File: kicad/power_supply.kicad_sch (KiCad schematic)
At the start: 14 parts, among them U3 LMR38010

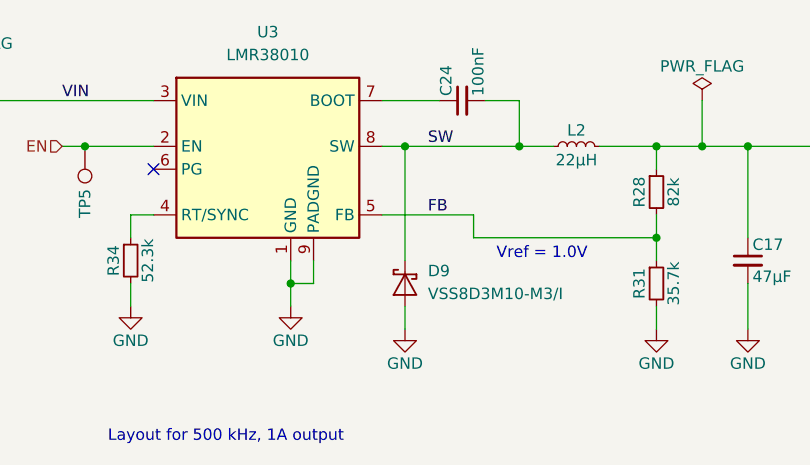
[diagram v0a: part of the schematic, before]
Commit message: power terminals THT, add mask
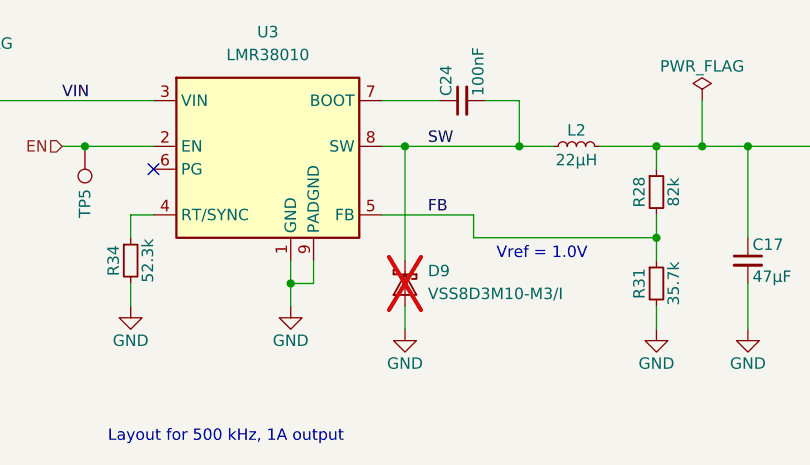
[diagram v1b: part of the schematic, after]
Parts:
- D9: now not fitted; now left out of the parts list
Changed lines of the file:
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@@
 		(unit 1)
 		(exclude_from_sim no)
-		(in_bom yes)
+		(in_bom no)
 		(on_board yes)
-		(dnp no)
+		(dnp yes)
 		(fields_autoplaced yes)
 		(property "Reference" "D9"
